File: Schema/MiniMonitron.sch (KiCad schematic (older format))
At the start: 41 parts, among them J1 CONN_01X02, J10 CONN_01X02, J2 CONN_02X20, J3 CONN_02X20, J4 CONN_01X02, J5 CONN_01X02, J6 CONN_01X02, J7 CONN_01X02, J8 CONN_01X02, J9 CONN_01X02, P1 conn2x18pcie, U1 PCF2129AT, U2 H11AA1M, U3 MCP2551-I/SN, U4 AXB050X43-SRZ, U5 LM1084IT-ADJ/NOPB

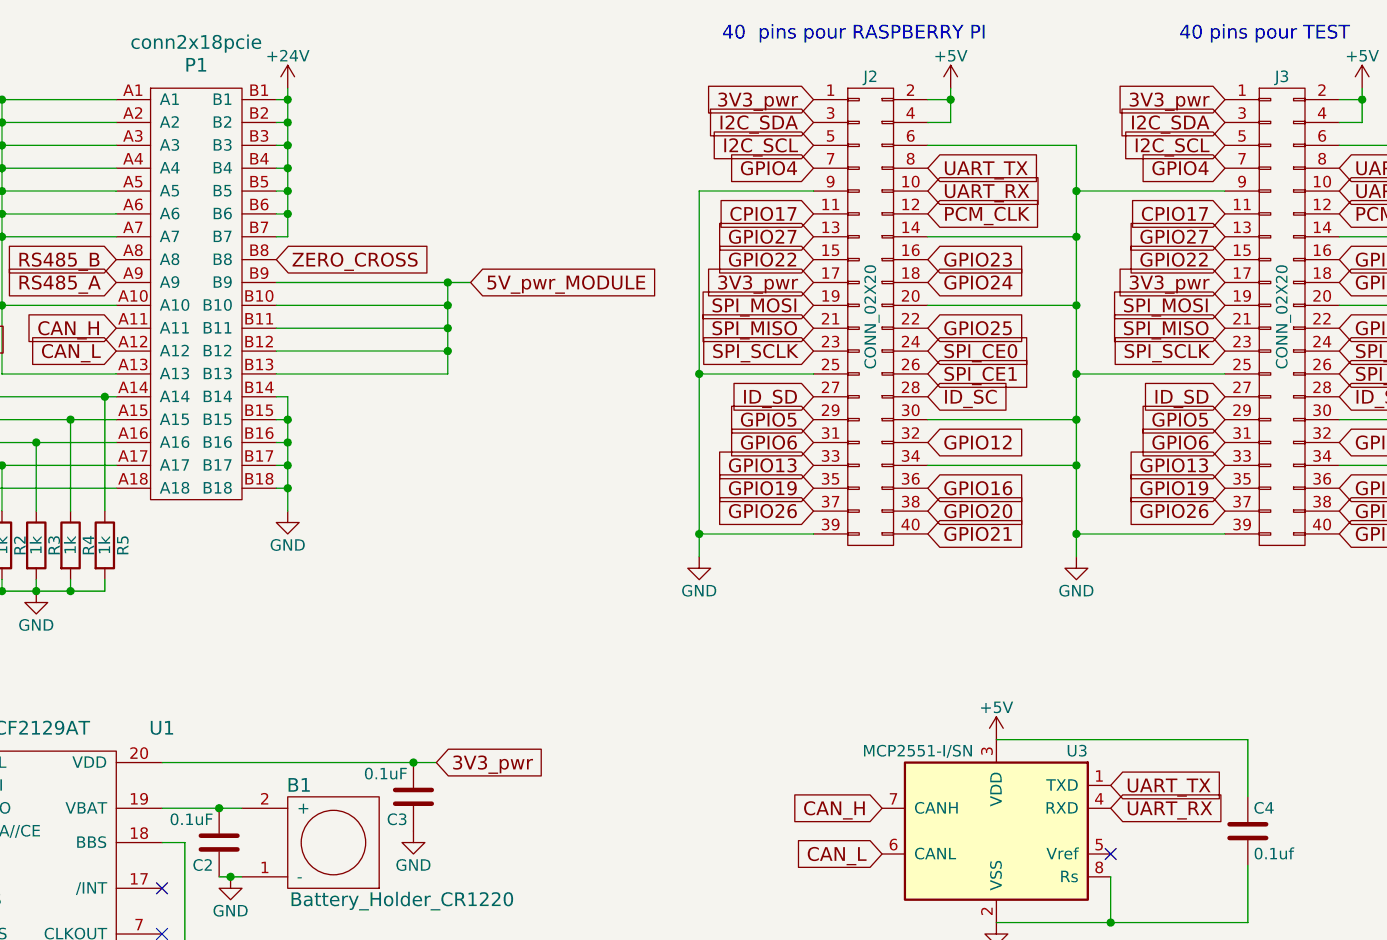
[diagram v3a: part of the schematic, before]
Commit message: Placement des pièces sur le PCB + commencement du routage
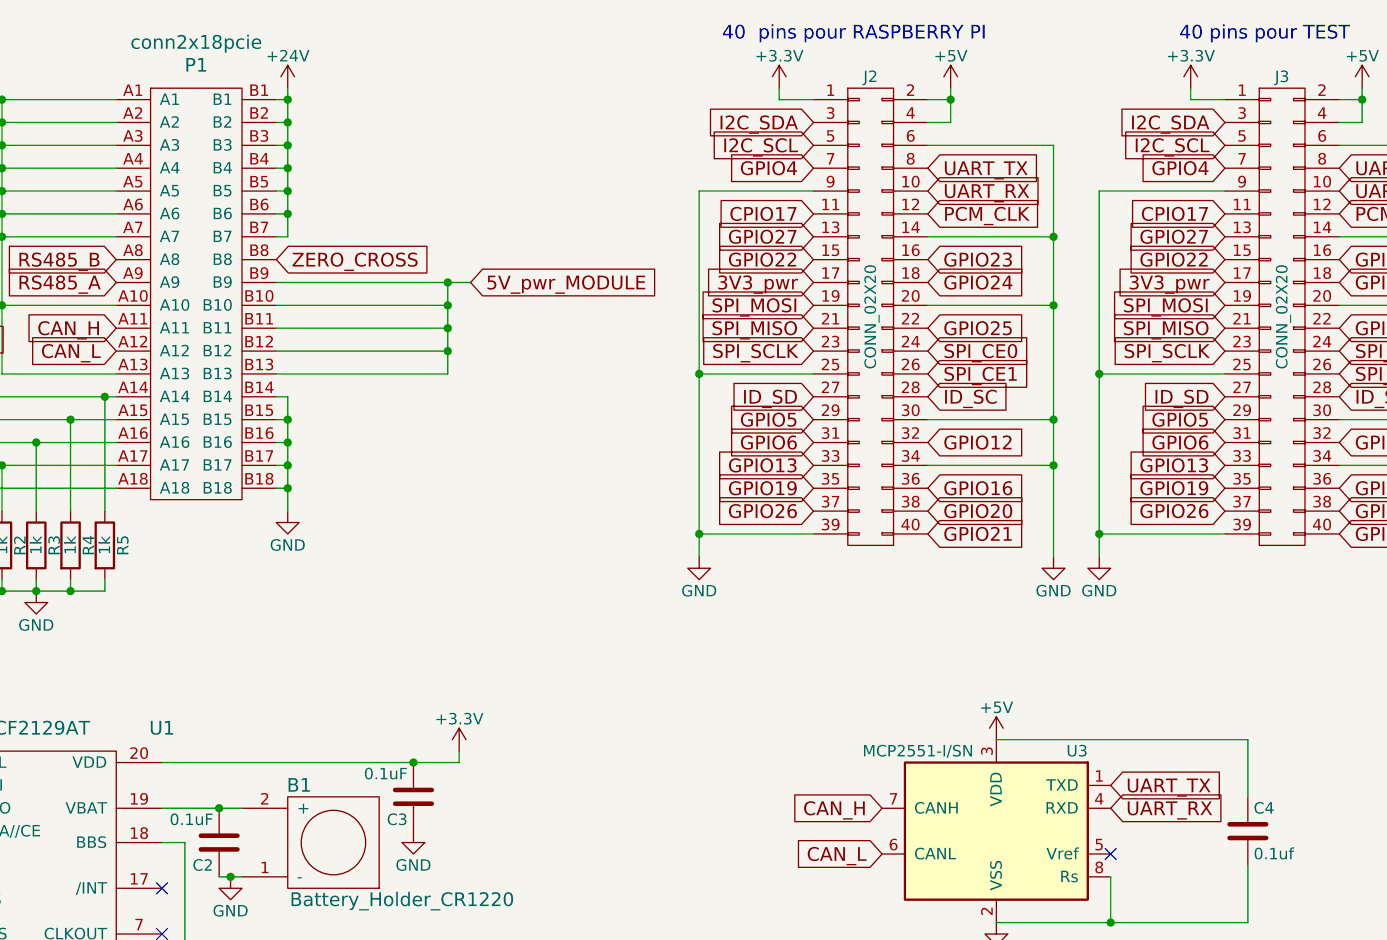
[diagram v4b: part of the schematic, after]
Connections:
- net +3V3: now also C3.2, J2.1 (P1), J3.1 (P1), U1.20 (VDD)
- net 3V3_pwr: no longer C3.2, J2.1 (P1), J3.1 (P1), U1.20 (VDD)
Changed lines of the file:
@@
 	1    0    0    -1
 $EndComp
-Text GLabel 3300 3800 2    60   Input ~ 0
-3V3_pwr
 $Comp
 L C C2
@@
 	1    0    0    -1
 $EndComp
-Text GLabel 4950 900  0    60   Input ~ 0
-3V3_pwr
-Text GLabel 6750 900  0    60   Input ~ 0
-3V3_pwr
 $Comp
 L AXB050X43-SRZ U4
@@
 L GND #PWR027
 U 1 1 5A8B4861
-P 6100 2900
-F 0 "#PWR027" H 6100 2650 50  0001 C CNN
-F 1 "GND" H 6100 2750 50  0000 C CNN
-F 2 "" H 6100 2900 50  0001 C CNN
-F 3 "" H 6100 2900 50  0001 C CNN
-	1    6100 2900
+P 6000 2900
+F 0 "#PWR027" H 6000 2650 50  0001 C CNN
+F 1 "GND" H 6000 2750 50  0000 C CNN
+F 2 "" H 6000 2900 50  0001 C CNN
+F 3 "" H 6000 2900 50  0001 C CNN
+	1    6000 2900
 	1    0    0    -1
 $EndComp
@@
 	2350 4300 2450 4300
 Wire Wire Line
-	2100 3800 3300 3800
+	2100 3800 3400 3800
 Connection ~ 3200 3800
 Connection ~ 2400 4300
@@
 Wire Wire Line
 	8900 1850 8100 1850
-Wire Wire Line
-	6750 1300 6100 1300
-Wire Wire Line
-	6100 1100 6100 2900
-Wire Wire Line
-	6750 2800 6100 2800
-Connection ~ 6100 2800
-Wire Wire Line
-	6750 2100 6100 2100
-Connection ~ 6100 2100
-Wire Wire Line
-	5450 1100 6100 1100
-Connection ~ 6100 1300
-Wire Wire Line
-	5450 1500 6100 1500
-Connection ~ 6100 1500
-Wire Wire Line
-	5450 1800 6100 1800
-Connection ~ 6100 1800
-Wire Wire Line
-	5450 2500 6100 2500
-Connection ~ 6100 2500
-Wire Wire Line
-	5450 2300 6100 2300
-Connection ~ 6100 2300
 Wire Wire Line
 	4950 1300 4450 1300
@@
 	1    0    0    -1
 $EndComp
+$Comp
+L +3.3V #PWR031
+U 1 1 5A902936
+P 6600 850
+F 0 "#PWR031" H 6600 700 50  0001 C CNN
+F 1 "+3.3V" H 6600 990 50  0000 C CNN
+F 2 "" H 6600 850 50  0001 C CNN
+F 3 "" H 6600 850 50  0001 C CNN
+	1    6600 850
+	1    0    0    -1
+$EndComp
+$Comp
+L +3.3V #PWR032
+U 1 1 5A902B8D
+P 4800 850
+F 0 "#PWR032" H 4800 700 50  0001 C CNN
+F 1 "+3.3V" H 4800 990 50  0000 C CNN
+F 2 "" H 4800 850 50  0001 C CNN
+F 3 "" H 4800 850 50  0001 C CNN
+	1    4800 850
+	1    0    0    -1
+$EndComp
+Wire Wire Line
+	6750 900  6600 900
+Wire Wire Line
+	6600 900  6600 850
+Wire Wire Line
+	4950 900  4800 900
+Wire Wire Line
+	4800 900  4800 850
+$Comp
+L +3.3V #PWR033
+U 1 1 5A903059
+P 3400 3750
+F 0 "#PWR033" H 3400 3600 50  0001 C CNN
+F 1 "+3.3V" H 3400 3890 50  0000 C CNN
+F 2 "" H 3400 3750 50  0001 C CNN
+F 3 "" H 3400 3750 50  0001 C CNN
+	1    3400 3750
+	1    0    0    -1
+$EndComp
+Wire Wire Line
+	3400 3800 3400 3750
+$Comp
+L GND #PWR?
+U 1 1 5A904304
+P 6200 2900
+F 0 "#PWR?" H 6200 2650 50  0001 C CNN
+F 1 "GND" H 6200 2750 50  0000 C CNN
+F 2 "" H 6200 2900 50  0001 C CNN
+F 3 "" H 6200 2900 50  0001 C CNN
+	1    6200 2900
+	1    0    0    -1
+$EndComp
+Wire Wire Line
+	6000 2900 6000 1100
+Connection ~ 6000 1500
+Wire Wire Line
+	6000 1100 5450 1100
+Wire Wire Line
+	5450 1500 6000 1500
+Wire Wire Line
+	5450 1800 6000 1800
+Connection ~ 6000 1800
+Wire Wire Line
+	5450 2300 6000 2300
+Connection ~ 6000 2300
+Wire Wire Line
+	5450 2500 6000 2500
+Connection ~ 6000 2500
+Wire Wire Line
+	6750 1300 6200 1300
+Wire Wire Line
+	6200 1300 6200 2900
+Wire Wire Line
+	6750 2100 6200 2100
+Connection ~ 6200 2100
+Wire Wire Line
+	6750 2800 6200 2800
+Connection ~ 6200 2800
 $EndSCHEMATC

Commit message: PCB terminé et envoyé, fichiers gerber crées + création du dossier Documentations avec le document du manuel technique
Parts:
- B1: footprint mini_monitron:keystone_1220 -> mini_monitron:Keystone_CR1220_SMD
- J2: footprint mini_monitron:IDC_Header_Straight_40pins -> mini_monitron:Pin_Header_Straight_2x20_Pitch2.54mm
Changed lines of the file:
@@
 F 0 "J2" H 5200 2900 50  0000 C CNN
 F 1 "CONN_02X20" V 5200 1850 50  0000 C CNN
-F 2 "mini_monitron:IDC_Header_Straight_40pins" H 5200 900 50  0001 C CNN
+F 2 "mini_monitron:Pin_Header_Straight_2x20_Pitch2.54mm" H 5200 900 50  0001 C CNN
 F 3 "" H 5200 900 50  0001 C CNN
 	1    5200 1850
@@
 F 0 "B1" H 3400 3900 60  0000 C CNN
 F 1 "Battery_Holder_CR1220" H 2950 4400 60  0000 C CNN
-F 2 "mini_monitron:keystone_1220" H 3050 4350 60  0001 C CNN
+F 2 "mini_monitron:Keystone_CR1220_SMD" H 3050 4350 60  0001 C CNN
 F 3 "" H 3050 4350 60  0001 C CNN
 	1    3050 4350
@@
 	3400 3800 3400 3750
 $Comp
-L GND #PWR?
+L GND #PWR034
 U 1 1 5A904304
 P 6200 2900
-F 0 "#PWR?" H 6200 2650 50  0001 C CNN
+F 0 "#PWR034" H 6200 2650 50  0001 C CNN
 F 1 "GND" H 6200 2750 50  0000 C CNN
 F 2 "" H 6200 2900 50  0001 C CNN

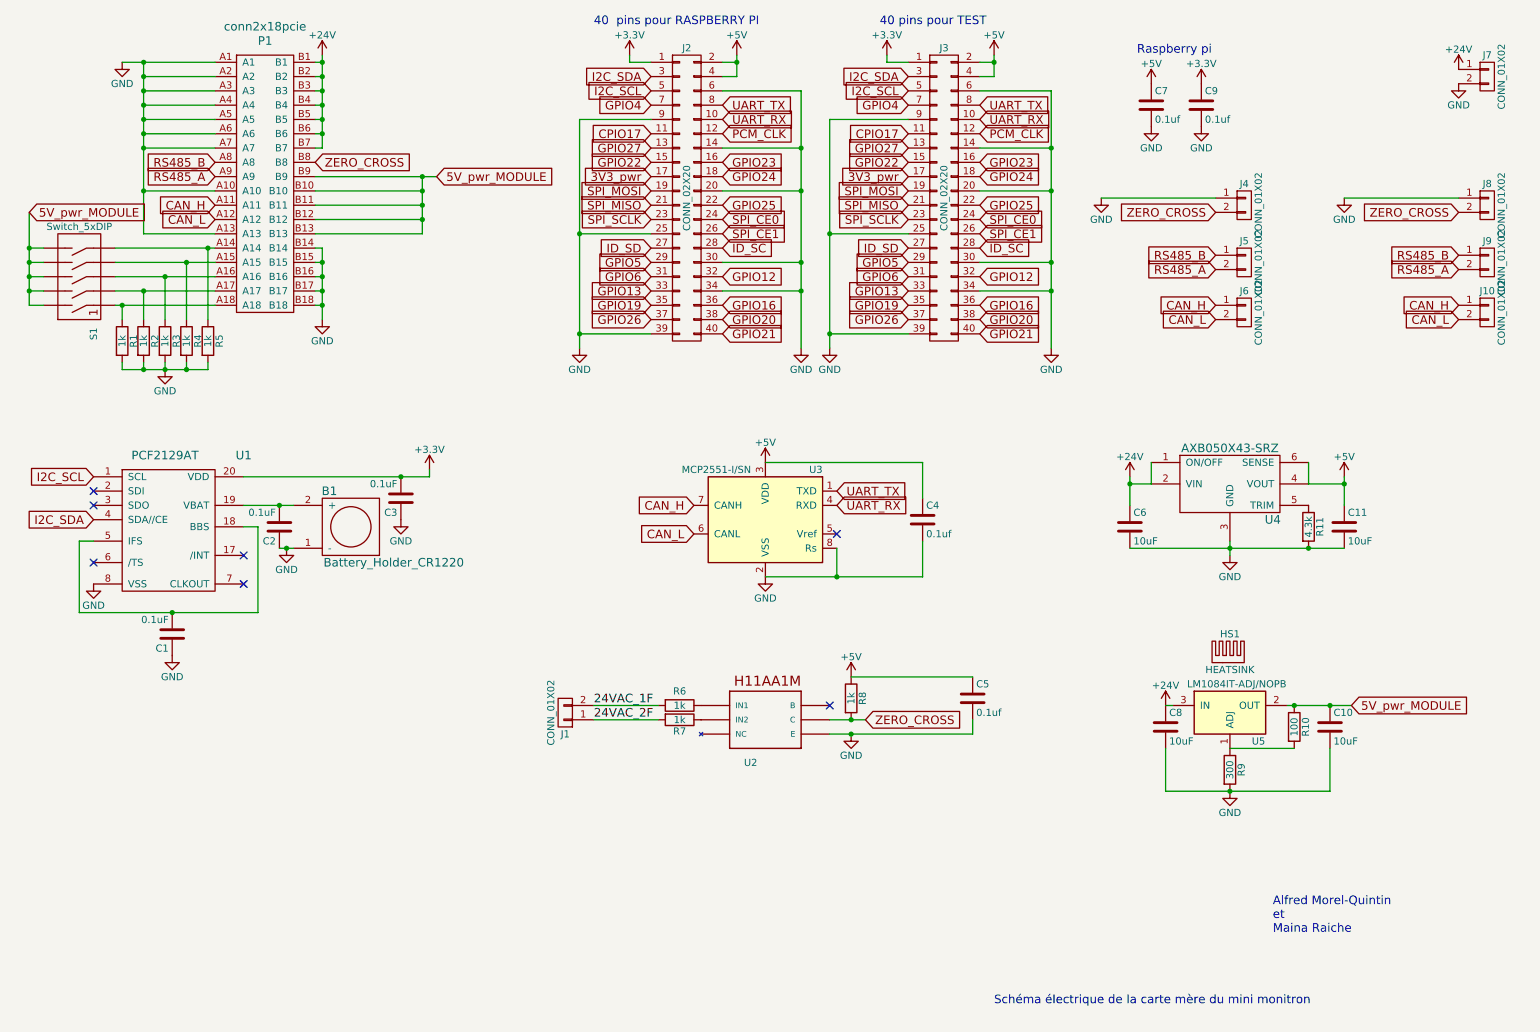
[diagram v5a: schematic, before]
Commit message: Correction du PCB + nouveau fichier Gerber
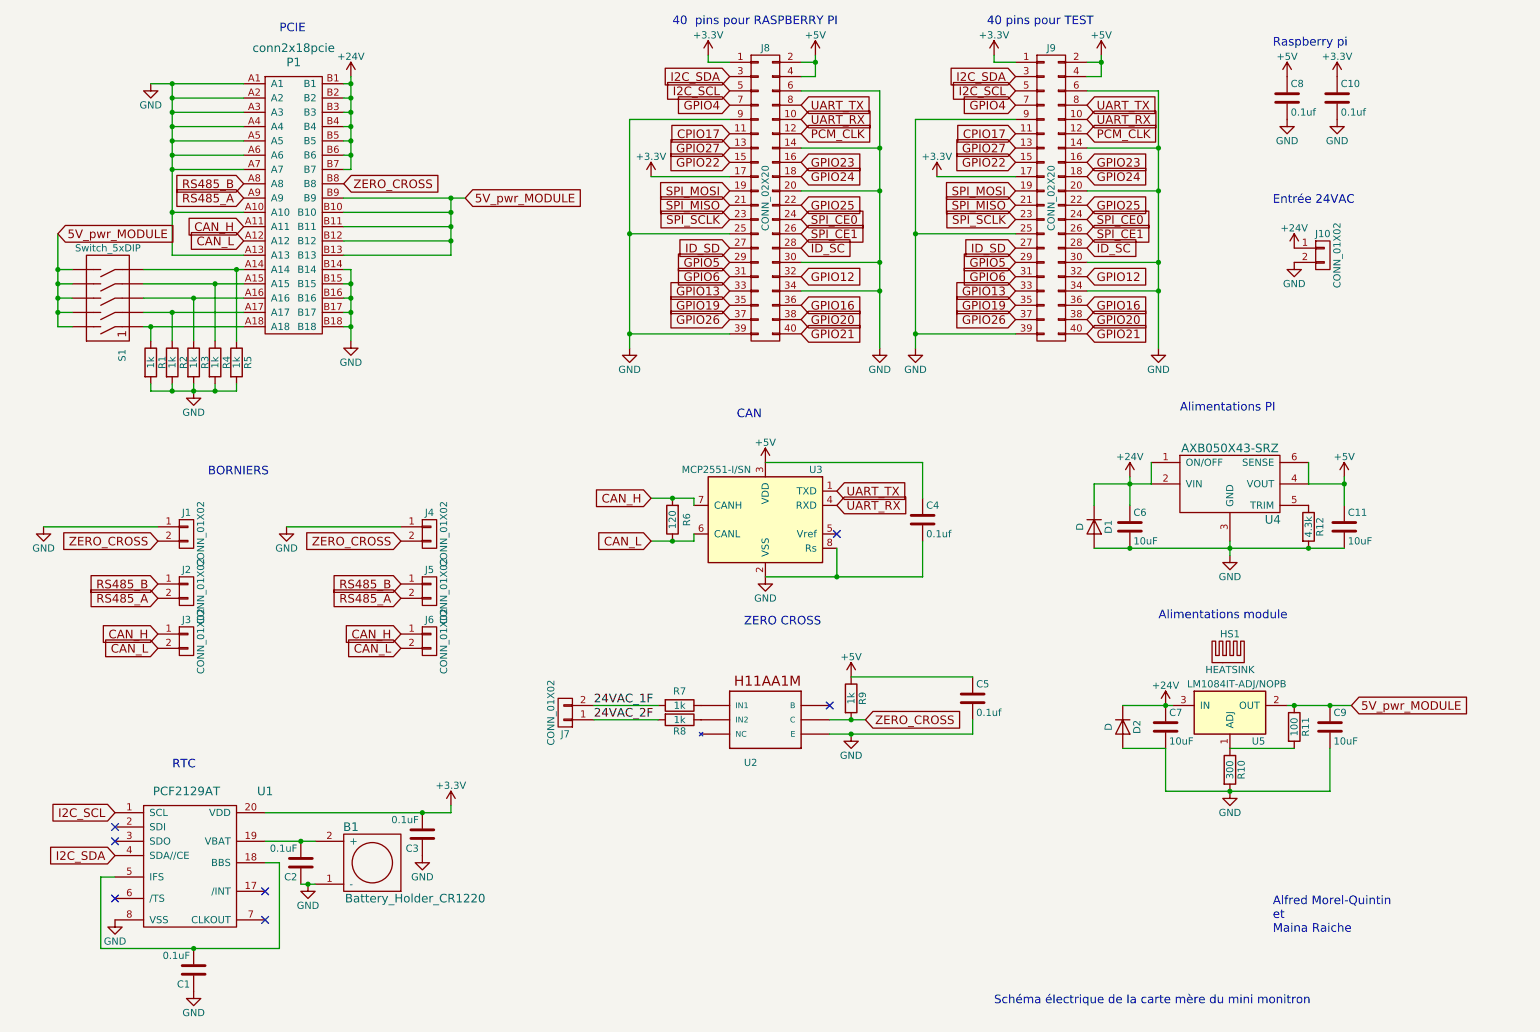
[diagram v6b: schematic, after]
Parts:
- added D1, D2: D, mini_monitron:D_0805, symbol D
- added R6: 120, mini_monitron:R_0805_HandSoldering, symbol R
- P1: footprint mini_monitron:pci-x_conn-x1_Vertical -> mini_monitron:pci-x_conn-x1_Vertical_back
- renumbered C9 to C10, C8 to C7, C7 to C8, C10 to C9, J4 to J1, J7 to J10, J5 to J2, J6 to J3, J8 to J4, J9 to J5, J10 to J6, J1 to J7, J2 to J8, J3 to J9, R9 to R10, R10 to R11, R11 to R12, R6 to R7, R7 to R8, R8 to R9
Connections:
- net 3V3_pwr is gone; now on net +3V3: J8.17 (P17), J9.17 (P17)
- net +24V: now also D1.1 (K), D2.1 (K)
- net CAN_H: now also R6.2
- net CAN_L: now also R6.1
- net GND: now also D1.2 (A), D2.2 (A)
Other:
- note added: "Alimentations PI\n\n"
- note added: "Alimentations module\n\n\n"
- note added: "BORNIERS"
- note added: "CAN"
- note added: "Entrée 24VAC\n"
- note added: "PCIE"
- note added: "RTC"
- note added: "ZERO CROSS"
- moved on the sheet: B1, C1, C10, C2, C3, C8, J1, J10, J2, J3, J4, J5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

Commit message: PCB final + avancement du manuel technique
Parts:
- R12: value 4.3k -> 10k
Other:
- note added: "Entrée 24VDC\n"
- note removed: "Entrée 24VAC\n"
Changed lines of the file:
@@
 P 9550 4150
 F 0 "R12" V 9630 4150 50  0000 C CNN
-F 1 "4.3k" V 9550 4150 50  0000 C CNN
+F 1 "10k" V 9550 4150 50  0000 C CNN
 F 2 "mini_monitron:R_0805_HandSoldering" V 9480 4150 50  0001 C CNN
 F 3 "" H 9550 4150 50  0001 C CNN
@@
 Text Notes 8650 3450 0    60   ~ 0
 Alimentations PI\n\n
-Text Notes 5550 3400 0    60   ~ 0
+Text Notes 5650 3400 0    60   ~ 0
 CAN
-Text Notes 5600 4850 0    60   ~ 0
+Text Notes 5450 5000 0    60   ~ 0
 ZERO CROSS
 Text Notes 1600 5850 0    60   ~ 0
@@
 BORNIERS
 Text Notes 9300 1900 0    60   ~ 0
-Entrée 24VAC\n
+Entrée 24VDC\n
 Text Notes 8500 5000 0    60   ~ 0
 Alimentations module\n\n\n
